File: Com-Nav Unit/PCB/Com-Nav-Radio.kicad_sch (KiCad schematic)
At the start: 116 parts, among them J1 GT-USB-7055, J2 Conn_02x05_Odd_Even, J3 Conn_01x04_Pin, Q10 AO3401A, Q2 AO3401A, Q3 AO3401A, Q4 AO3401A, Q5 AO3401A, Q6 AO3401A, Q7 AO3401A, Q8 AO3401A, Q9 AO3401A, SW3 SW_Push, SW4 SW_Push, SW5 SW_Push, SW6 SW_Push, U1 STM32F411CEUx, U10 FJ2352, U11 FJ2352, U12 FJ2352, U13 FJ2352, U14 FJ2352, U15 74HC595, U16 74HC595, U17 ULN2003A, U18 ULN2003A, U19 ULN2003A, U2 74HC595, U20 ULN2003A, U21 ULN2003A, U22 USBLC6-2SC6, U3 74HC595, U4 XC6206P332MR, U5 FJ2352, U6 FJ2352, U7 FJ2352, U8 FJ2352, U9 FJ2352, Y2 25 MHz

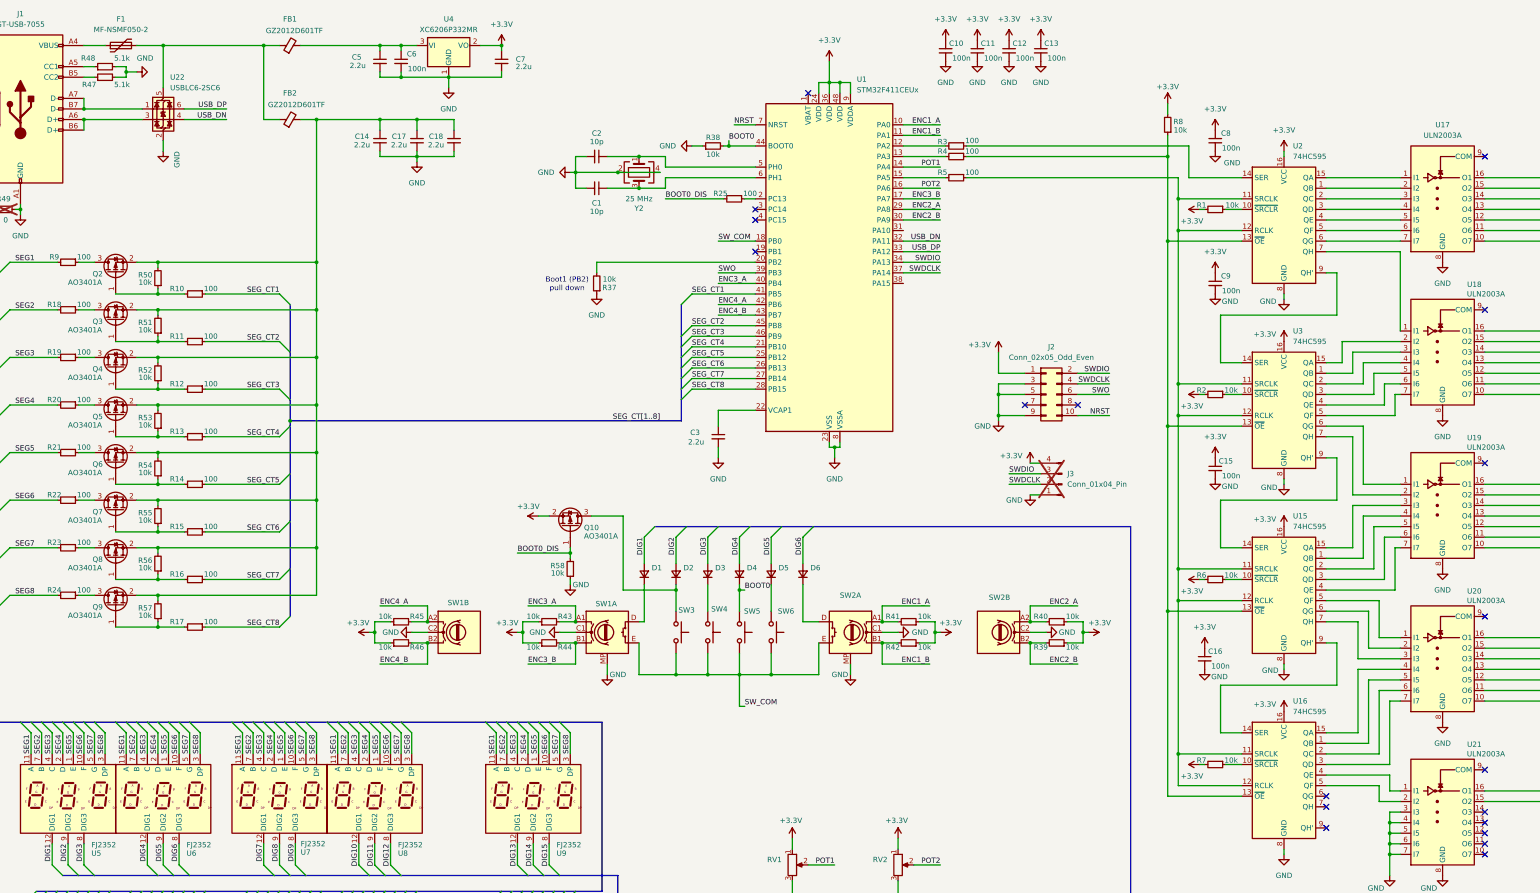
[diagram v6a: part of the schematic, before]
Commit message: PCB - work on schematic, initial board placement
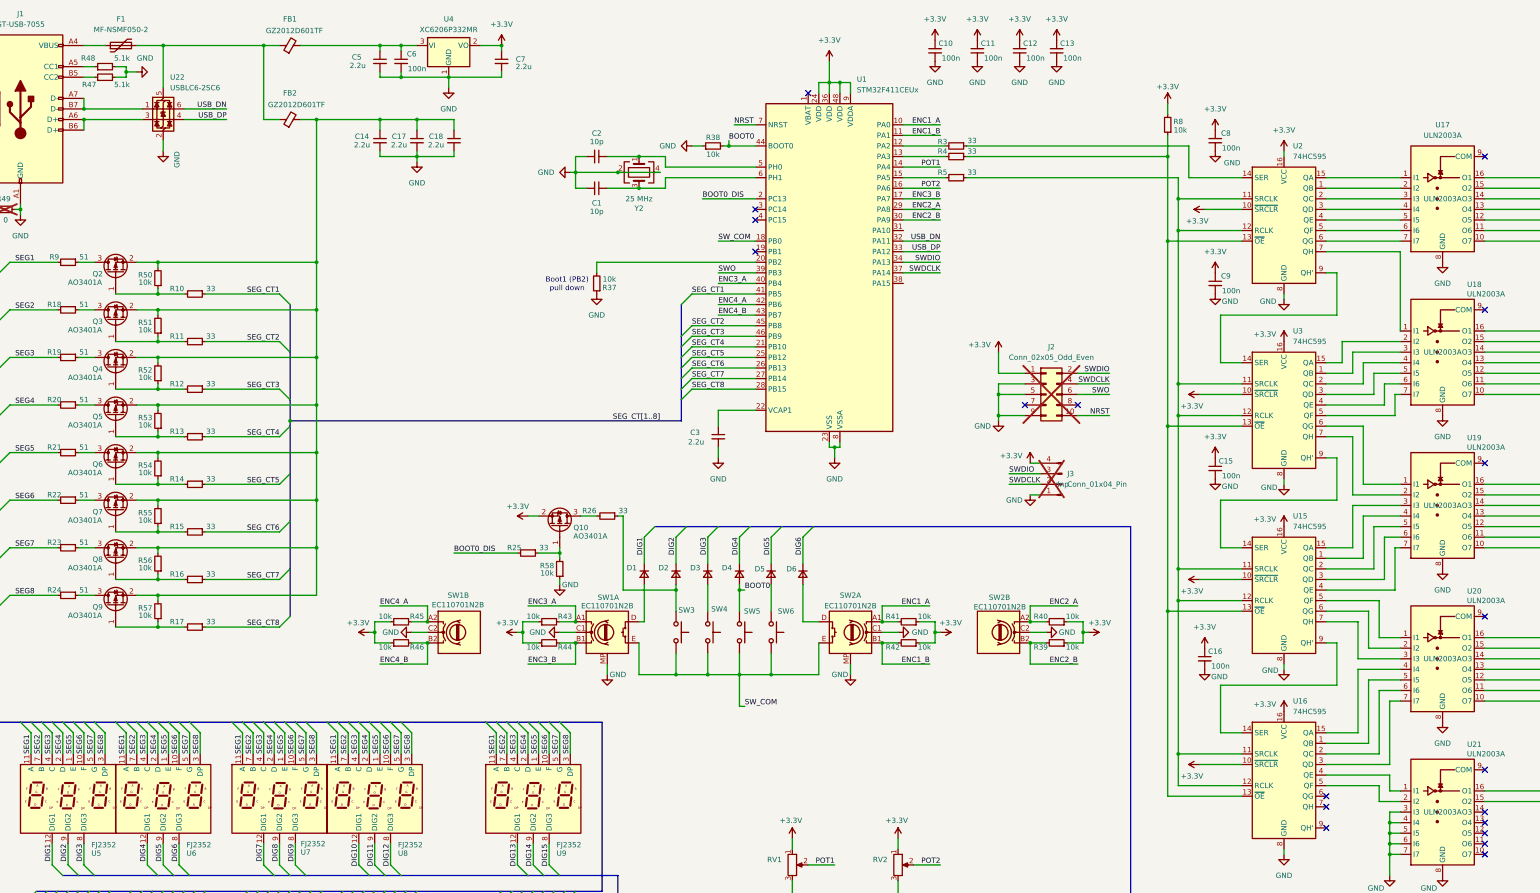
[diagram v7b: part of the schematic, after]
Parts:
- removed R1, R2, R6, R7: 10k, Resistor_SMD:R_0603_1608Metric, symbol Device:R_Small
- added R26: 33, Resistor_SMD:R_0402_1005Metric, symbol Device:R_Small
- C1, C2: PN (none) -> CL05C100JB5NNNC
- C10, C11, C12, C13, C15, C16, C6, C8, C9: footprint Capacitor_SMD:C_0603_1608Metric -> Capacitor_SMD:C_0402_1005Metric; PN (none) -> CL05B104KO5NNNC
- C14, C17, C18, C3, C5, C7: PN (none) -> CL10A225KO8NNNC
- D1, D2, D3, D4, D5, D6: value SM4007PL -> 1N5819WS; footprint Diode_SMD:D_SOD-123F -> Diode_SMD:D_SOD-323; PN SM4007PL -> 1N5819WS
- J2: now not fitted
- J3: PN (none) -> dnp; now in the parts list
- Q10, Q2, Q3, Q4, Q5, Q6, Q7, Q8, Q9: PN (none) -> AO3401A
- R10, R11, R12, R13, R14, R15, R16, R17, R25, R3, R4, R5: value 100 -> 33; footprint Resistor_SMD:R_0603_1608Metric -> Resistor_SMD:R_0402_1005Metric; PN 0603WAF1000T5E -> 0402WGF330JTCE
- R18, R19, R20, R21, R22, R23, R24, R9: value 100 -> 51; footprint Resistor_SMD:R_0603_1608Metric -> Resistor_SMD:R_0805_2012Metric; PN 0603WAF1000T5E -> 0805W8F5100T5E
- R37, R38, R39, R40, R41, R42, R43, R44, R45, R46, R50, R51, R52, R53, R54, R55, R56, R57, R58, R8: footprint Resistor_SMD:R_0603_1608Metric -> Resistor_SMD:R_0402_1005Metric; PN 0603WAF1002T5E -> 0402WGF1002TCE
- R47, R48: footprint Resistor_SMD:R_0603_1608Metric -> Resistor_SMD:R_0402_1005Metric; PN (none) -> 0402WGF5101TCE
- R49: PN (none) -> dnp
- RV1, RV2: value R_Potentiometer -> RA0901N0X0D; footprint (none) -> Encoder:RA0901N0X0D-HA1; PN (none) -> RA0901N0X0D-HA1
- SW1, SW2: value ~ -> EC110701N2B; footprint (none) -> Encoder:EC11EBB24C03_EC110701N2B; PN (none) -> EC110701N2B
- SW3, SW4, SW5, SW6: PN (none) -> *** MAYBE CHANGE FOR SMD
- U17, U18, U19, U20, U21: PN (none) -> ULN2003A
- U22: PN (none) -> USBLC6-2SC6
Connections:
- net +3.3V: now also U15.10 (~{SRCLR}), U16.10 (~{SRCLR}), U2.10 (~{SRCLR}), U3.10 (~{SRCLR})
- net BOOT0: now also D4.2 (A); no longer D4.1 (K)
- net BOOT0_DIS: now also U1.2 (PC13); no longer Q10.1 (G), R58.2
- net DIG1: now also D1.1 (K); no longer D1.2 (A)
- net DIG2: now also D2.1 (K); no longer D2.2 (A)
- net DIG3: now also D3.1 (K); no longer D3.2 (A)
- net DIG4: now also D4.1 (K); no longer D4.2 (A)
- net DIG5: now also D5.1 (K); no longer D5.2 (A)
- net DIG6: now also D6.1 (K); no longer D6.2 (A)
- net USB_DN: now also U22.6 (I/O1); no longer U22.4 (I/O2)
- net USB_DP: now also U22.4 (I/O2); no longer U22.6 (I/O1)
- net at SW1.D: now also D1.2 (A); no longer D1.1 (K)
- net at SW4.2: now also D3.2 (A); no longer D3.1 (K)
- net at SW6.2: now also D5.2 (A); no longer D5.1 (K)
- net at SW2.D: now also D6.2 (A); no longer D6.1 (K)
- net at R25.1: now also Q10.1 (G), R58.2; no longer U1.2 (PC13)
- new net: D2.2 (A), R26.1, SW3.2
- new net: Q10.3 (D), R26.2
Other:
- moved on the sheet: C10, C12, C13, D1, D2, D3, D4, D5, D6, Q10, R25, R58

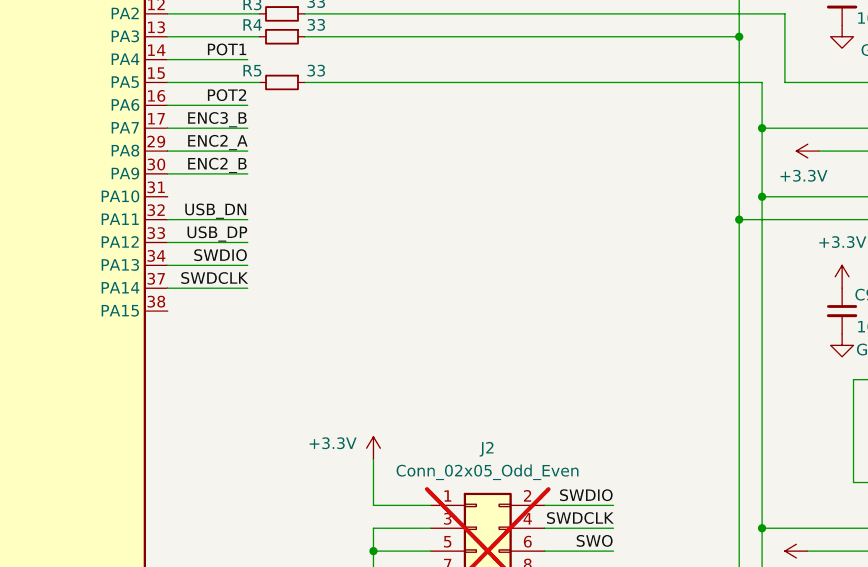
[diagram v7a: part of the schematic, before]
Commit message: PCB - Sketch routing of the 7 segments
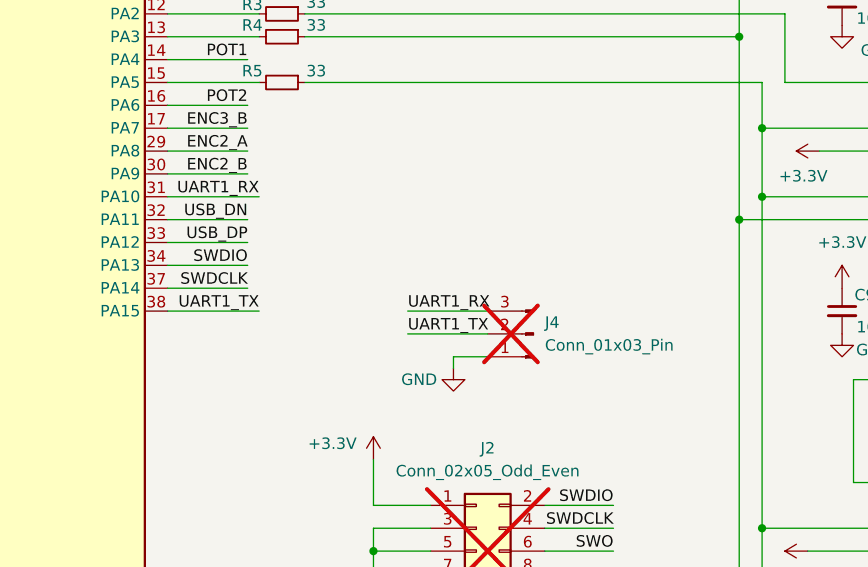
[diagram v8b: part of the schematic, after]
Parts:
- added J4: Conn_01x03_Pin, Connector_PinHeader_2.54mm:PinHeader_1x03_P2.54mm_Vertical, symbol Connector:Conn_01x03_Pin
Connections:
- net GND: now also J4.1 (Pin_1)
- net UART1_RX: now reaches U1.31 (PA10)
- net UART1_RX: now also J4.3 (Pin_3)
- net UART1_TX: now reaches U1.38 (PA15)
- net UART1_TX: now also J4.2 (Pin_2)
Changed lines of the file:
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@@
 	(wire
 		(pts
+			(xy 247.65 80.01) (xy 257.81 80.01)
+		)
+		(stroke
+			(width 0)
+			(type default)
+		)
+	)
+	(wire
+		(pts
 			(xy 106.68 120.65) (xy 106.68 132.08)
 		)
@@
 		)
 	)
+	(wire
+		(pts
+			(xy 274.32 80.01) (xy 283.21 80.01)
+		)
+		(stroke
+			(width 0)
+			(type default)
+		)
+	)
 	(bus
 		(pts
@@
 	(wire
 		(pts
+			(xy 279.4 85.09) (xy 283.21 85.09)
+		)
+		(stroke
+			(width 0)
+			(type default)
+		)
+	)
+	(wire
+		(pts
 			(xy 49.53 143.51) (xy 53.34 143.51)
 		)
@@
 	(wire
 		(pts
+			(xy 247.65 67.31) (xy 257.81 67.31)
+		)
+		(stroke
+			(width 0)
+			(type default)
+		)
+	)
+	(wire
+		(pts
 			(xy 196.85 105.41) (xy 212.09 105.41)
 		)
@@
 		)
 	)
+	(wire
+		(pts
+			(xy 279.4 86.36) (xy 279.4 85.09)
+		)
+		(stroke
+			(width 0)
+			(type default)
+		)
+	)
 	(bus
 		(pts
@@
 		)
 	)
+	(wire
+		(pts
+			(xy 274.32 82.55) (xy 283.21 82.55)
+		)
+		(stroke
+			(width 0)
+			(type default)
+		)
+	)
 	(label "SEG7"
 		(at 165.1 193.04 90)
@@
 		)
 	)
+	(label "UART1_TX"
+		(at 274.32 82.55 0)
+		(effects
+			(font
+				(size 1.27 1.27)
+			)
+			(justify left bottom)
+		)
+	)
 	(label "SEG5"
 		(at 34.29 120.65 0)
@@
 		)
 	)
+	(label "UART1_TX"
+		(at 257.81 80.01 180)
+		(effects
+			(font
+				(size 1.27 1.27)
+			)
+			(justify right bottom)
+		)
+	)
 	(label "SWDCLK"
 		(at 256.54 77.47 180)
@@
 		)
 	)
+	(label "UART1_RX"
+		(at 257.81 67.31 180)
+		(effects
+			(font
+				(size 1.27 1.27)
+			)
+			(justify right bottom)
+		)
+	)
 	(label "SEG_CT7"
 		(at 97.79 151.13 180)
@@
 		)
 	)
+	(label "UART1_RX"
+		(at 274.32 80.01 0)
+		(effects
+			(font
+				(size 1.27 1.27)
+			)
+			(justify left bottom)
+		)
+	)
 	(label "DIG28"
 		(at 410.21 180.34 180)
@@
 	)
 	(symbol
+		(lib_id "Connector:Conn_01x03_Pin")
+		(at 288.29 82.55 180)
+		(unit 1)
+		(exclude_from_sim no)
+		(in_bom yes)
+		(on_board yes)
+		(dnp yes)
+		(fields_autoplaced yes)
+		(property "Reference" "J4"
+			(at 289.56 81.2799 0)
+			(effects
+				(font
+					(size 1.27 1.27)
+				)
+				(justify right)
+			)
+		)
+		(property "Value" "Conn_01x03_Pin"
+			(at 289.56 83.8199 0)
+			(effects
+				(font
+					(size 1.27 1.27)
+				)
+				(justify right)
+			)
+		)
+		(property "Footprint" "Connector_PinHeader_2.54mm:PinHeader_1x03_P2.54mm_Vertical"
+			(at 288.29 82.55 0)
+			(effects
+				(font
+					(size 1.27 1.27)
+				)
+				(hide yes)
+			)
+		)
+		(property "Datasheet" "~"
+			(at 288.29 82.55 0)
+			(effects
+				(font
+					(size 1.27 1.27)
+				)
+				(hide yes)
+			)
+		)
+		(property "Description" "Generic connector, single row, 01x03, script generated"
+			(at 288.29 82.55 0)
+			(effects
+				(font
+					(size 1.27 1.27)
+				)
+				(hide yes)
+			)
+		)
+		(pin "3"
+		)
+		(pin "1"
+		)
+		(pin "2"
+		)
+		(instances
+			(project ""
+				(path "/69049761-9f2d-47f8-b9f8-414f51a5cecf"
+					(reference "J4")
+					(unit 1)
+				)
+			)
+		)
+	)
+	(symbol
 		(lib_id "power:+3.3V")
 		(at 270.51 96.52 0)
@@
 					(unit 1)
 				)
+			)
+		)
+	)
+	(symbol
+		(lib_id "power:GND")
+		(at 279.4 86.36 0)
+		(unit 1)
+		(exclude_from_sim no)
+		(in_bom yes)
+		(on_board yes)
+		(dnp no)
+		(property "Reference" "#PWR077"
+			(at 279.4 92.71 0)
+			(effects
+				(font
+					(size 1.27 1.27)
+				)
+				(hide yes)
+			)
+		)
+		(property "Value" "GND"
+			(at 275.59 87.63 0)
+			(effects
+				(font
+					(size 1.27 1.27)
+				)
+			)
+		)
+		(property "Footprint" ""
+			(at 279.4 86.36 0)
+			(effects
+				(font
+					(size 1.27 1.27)
+				)
+				(hide yes)
+			)
+		)
+		(property "Datasheet" ""
+			(at 279.4 86.36 0)
+			(effects
+				(font
+					(size 1.27 1.27)
+				)
+				(hide yes)
+			)
+		)
+		(property "Description" ""
+			(at 279.4 86.36 0)
+			(effects
+				(font
+					(size 1.27 1.27)
+				)
+			)
+		)
+		(pin "1"
+		)
+		(instances
+			(project "Com-Nav-Radio"
+				(path "/69049761-9f2d-47f8-b9f8-414f51a5cecf"
+					(reference "#PWR077")
+					(unit 1)
+				)
